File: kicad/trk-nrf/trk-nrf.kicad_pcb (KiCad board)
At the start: 4 copper layers, 23.2 x 22 mm, 46 parts, among them J1 Conn_02x05_Odd_Even, J2 Conn_01x20_Pin, U1 nRF9151-LAXX, U2 CDCE6214RGER, U3 TPS631010YBGR, U4 TPS631010YBGR, X1 TG2520SMN-xx.xxxxxxMhz-xxxxNM

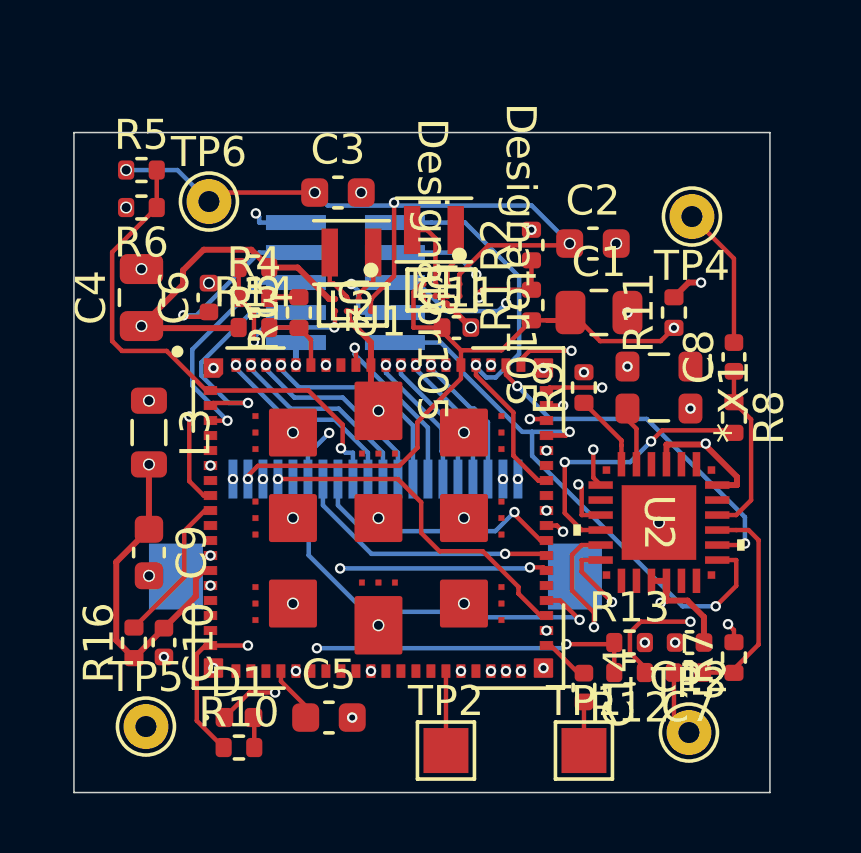
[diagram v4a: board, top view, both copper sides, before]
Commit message: Board detailed routing by Estifanos Nega
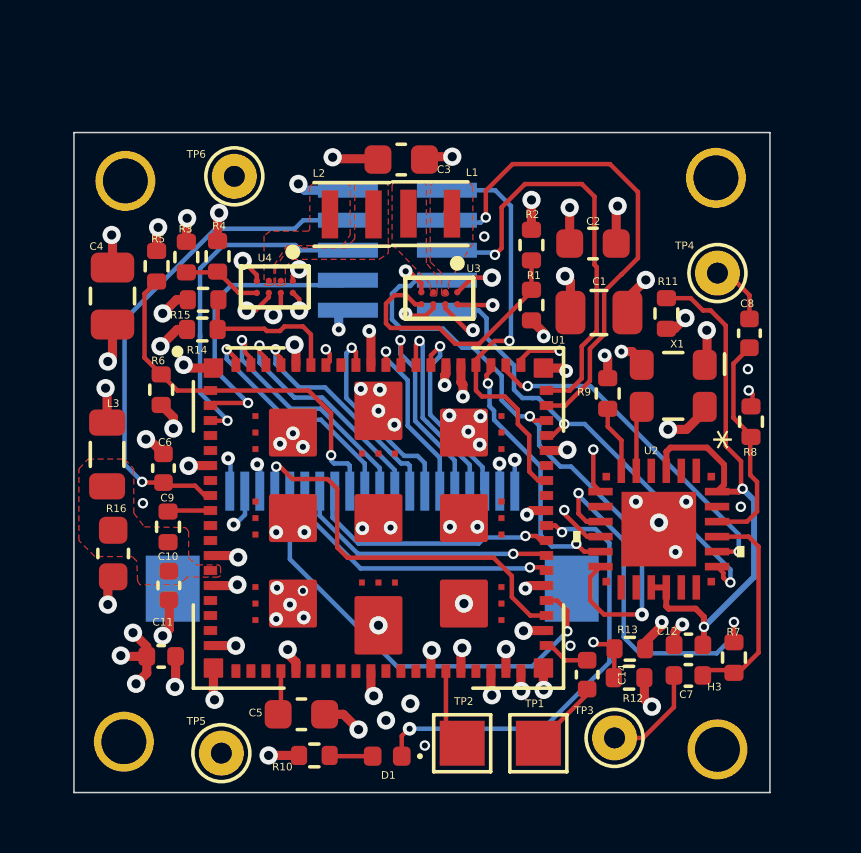
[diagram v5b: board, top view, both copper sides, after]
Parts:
- added H1: MountingHole_Pad_MP, MountingHole:MountingHole_2.2mm_M2_ISO7380_Pad, F.Cu at (171.4, 89.5)
- added H2: MountingHole_Pad_MP, MountingHole:MountingHole_2.2mm_M2_ISO7380_Pad, F.Cu at (151.7, 108.3)
- added H3: MountingHole_Pad_MP, MountingHole:MountingHole_2.2mm_M2_ISO7380_Pad, F.Cu at (171.4, 108.6)
- added H4: MountingHole_Pad_MP, MountingHole:MountingHole_2.2mm_M2_ISO7380_Pad, F.Cu at (151.7, 89.6)
- moved C11 14.7 mm to (152.9, 105.5), turned to 180 degrees
- moved R6 6.11 mm to (152.9, 96.6), turned to -90 degrees
- moved C6 5.89 mm to (153.0, 99.2)
- moved D1 5.11 mm to (160.4, 108.8), turned to 180 degrees
- moved R16 4.03 mm to (153.1, 101.1)
- moved R5 3.25 mm to (152.8, 92.5), turned to -90 degrees
- moved R15 3.22 mm to (154.3, 93.6), turned to 180 degrees
- moved U4 2.67 mm to (156.7, 93.1)
- moved TP5 2.67 mm to (154.9, 108.7)
- moved R10 2.53 mm to (158.0, 108.8)
- moved TP3 2.49 mm to (168.0, 108.2)
- moved C3 2.38 mm to (160.9, 88.9)
- moved R3 2.28 mm to (153.7, 92.2), turned to -90 degrees
- moved TP4 2.07 mm to (171.4, 92.7)
- moved J1 2.04 mm to (160.8, 91.9)
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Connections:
- net Net-(U3-LX1) renamed /LX1
- net Net-(U3-LX2) renamed /LX2
- net Net-(U4-LX1) renamed /LX1.1
- net Net-(U4-LX2) renamed /LX1.2
- X1 pad 1: unconnected-(X1-NC-Pad1) -> GND
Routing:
- net +1.8V: track 60.2 -> 14.2 mm, vias 6 -> 12
- net GND: track 7.88 -> 45.8 mm, vias 45 -> 84
- net VBUS: track 35.3 -> 8.21 mm, vias 5 -> 8
- net +3.3V: track 18.4 -> 6.15 mm, vias 3 -> 6
- net /+3.3V_Ferrite: track 11.3 -> 0.06 mm, vias 1 -> 0
- net /PLL_GPIO4: track 17.5 -> 8.77 mm
- net /UART_TX: track 9.34 -> 16.2 mm, vias 2 -> 1
- net /FB_1.8: track 3.65 -> 8.97 mm, vias 1 -> 0
- net /nRF_nRESET: track 12.1 -> 16.9 mm, vias 2 -> 1
- net /MON_VBUS: track 17.3 -> 12.8 mm
- net /P0.28: track 13.5 -> 9.60 mm, vias 3 -> 1
- net Net-(U1-ENABLE): track 5.07 -> 1.38 mm
- net /SDA: track 19.5 -> 15.8 mm
- net /SWDIO: track 7.81 -> 11.4 mm
- net /FB_3.3: track 6.21 -> 2.65 mm, vias 2 -> 0
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- added copper zone on In2.Cu, net +1.8V
- added copper zone on In2.Cu, net +3.3V
- added copper zone on F.Cu, net /+3.3V_Ferrite
- added copper zone on F.Cu, net /LX1
- added copper zone on F.Cu, net /LX1.1
- added copper zone on F.Cu, net /LX1.2
- added copper zone on F.Cu, net /LX2
- added copper zone on In2.Cu, net VBUS
